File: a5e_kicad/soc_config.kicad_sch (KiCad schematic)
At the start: 18 parts, among them U2 IS25WP128-RHLE, U7 A5EB013B-B23B

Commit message: Schematic reorg step 9: ERC to zero
- Wires trimmed back to their last label or cap (SDM config lines, LPDDR4
  decoupling rows, PG pins); loose stubs and R29 leftovers removed
- Unused bus links removed: {iob6a}, {iobank_2aB}, {iob6c}, {phy} and the
  io_headers {jtag} (sheet pins, root buses, unnamed internal buses);
  {iob6b} bus tail trimmed

Netdiff: 0 renamed, 0 connectivity diffs. ERC 21 -> 0. PCB unchanged, DRC parity 0.
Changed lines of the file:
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@@
 	(wire
 		(pts
-			(xy 193.04 68.58) (xy 210.82 68.58)
+			(xy 198.12 68.58) (xy 210.82 68.58)
 		)
 		(stroke
@@
 	(wire
 		(pts
-			(xy 193.04 81.28) (xy 210.82 81.28)
+			(xy 198.12 81.28) (xy 210.82 81.28)
 		)
 		(stroke
@@
 	(wire
 		(pts
-			(xy 193.04 76.2) (xy 210.82 76.2)
+			(xy 198.12 76.2) (xy 210.82 76.2)
 		)
 		(stroke
@@
 	(wire
 		(pts
-			(xy 193.04 91.44) (xy 210.82 91.44)
+			(xy 198.12 91.44) (xy 210.82 91.44)
 		)
 		(stroke
@@
 	(wire
 		(pts
-			(xy 193.04 83.82) (xy 210.82 83.82)
+			(xy 198.12 83.82) (xy 210.82 83.82)
 		)
 		(stroke
@@
 	(wire
 		(pts
-			(xy 193.04 86.36) (xy 210.82 86.36)
-		)
-		(stroke
+			(xy 198.12 86.36) (xy 210.82 86.36)
+		)
+		(stroke

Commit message: QSPI: 22R series resistors R293-R298 at U7 on AS_CLK/nCSO0/DATA0-3, sim/qspi_si
- schematic: resistors inline in the U7 AS pin wires; U7 side on new *_sdm nets; R7 (CS# pull-up) on the U7 side,
  where it is placed; R12/R14 stay on the flash side
- board: 0201 (C155743) on F.Cu below U7 (x 165.8-167.6 y 125.9; x 160.8-162.6 y 128.6), In2 tracks cut at each
  resistor, U7-side copper renamed to the *_sdm nets; connections to the pads still to route
- sim/qspi_si: IBIS (Agilex SDM 1p8_io_d8s1, flash stand-in, 100 MHz, typ/min/max): no termination peaks
  2.0-2.6 V; 22R 1.69-2.15 V with clean edges; 33R and up stair-step in the threshold band
- also carries the board edits in progress (Ethernet routing)
- ERC 0, parity 0, DRC: only the 12 dangling cut ends are new
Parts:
- added R293, R294, R295, R296, R297, R298: 22R, Resistor_SMD:R_0201_0603Metric, symbol Device:R
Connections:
- net qspi_CLK: now also R293.1; no longer U7.CY69 (SDM_SDM_IO2_AVSTx8_DATA0_AS_CLK)
- net qspi_D0: now also R295.1; no longer U7.CN64 (SDM_SDM_IO4_AVSTx8_DATA1_AS_DATA0)
- net qspi_D1: now also R296.1; no longer U7.CK67 (SDM_SDM_IO1_AVSTx8_DATA2_AS_DATA1)
- net qspi_D2: now also R297.1; no longer U7.DC74 (SDM_SDM_IO3_AVSTx8_DATA3_AS_DATA2)
- net qspi_D3: now also R298.1; no longer U7.DC75 (SDM_SDM_IO6_AVSTx8_DATA4_AS_DATA3)
- net ~{qspi_CS}: now also R294.1; no longer R7.2, U7.BY71 (SDM_SDM_IO5_AS_nCSO0_MSEL0)
- new net qspi_CLK_sdm: R293.2, U7.CY69 (SDM_SDM_IO2_AVSTx8_DATA0_AS_CLK)
- new net qspi_D0_sdm: R295.2, U7.CN64 (SDM_SDM_IO4_AVSTx8_DATA1_AS_DATA0)
- new net qspi_D1_sdm: R296.2, U7.CK67 (SDM_SDM_IO1_AVSTx8_DATA2_AS_DATA1)
- new net qspi_D2_sdm: R297.2, U7.DC74 (SDM_SDM_IO3_AVSTx8_DATA3_AS_DATA2)
- new net qspi_D3_sdm: R298.2, U7.DC75 (SDM_SDM_IO6_AVSTx8_DATA4_AS_DATA3)
- new net ~{qspi_CS_sdm}: R294.2, R7.2, U7.BY71 (SDM_SDM_IO5_AS_nCSO0_MSEL0)

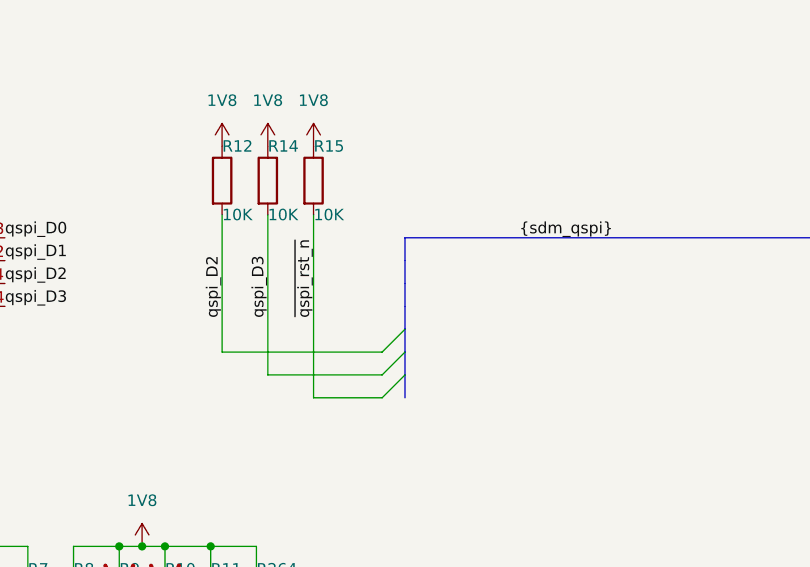
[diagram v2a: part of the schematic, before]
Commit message: Ethernet PHY passives to 0201, R27/R28 to 0402, preliminary RGMII routing
- 31 PHY passives on the hps_ethernet sheet 0402 -> 0201 (C24 22u stays
  0402): 100n C190183, 1u C272877, 27p C85899, 10k C473048,
  330R C516485, 4K7 C270346, 1K5 C270361, 2K49 C473476.
- Refclk bias R27/R28 0201 -> 0402 (C25120, 49.9R); R28 moved 0.1 mm
  to +x to clear the refclk_N meander.
- Preliminary RGMII routing: RX on F.Cu, TX on In2. Group spread
  TX 79 ps (TXD1 longest), RX 44 ps.
- Schematic sheets as saved by eeschema.
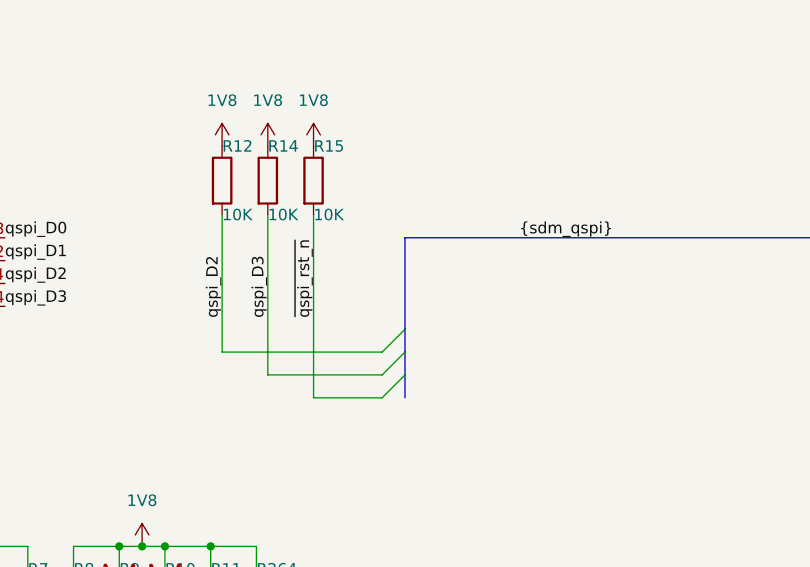
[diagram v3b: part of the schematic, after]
